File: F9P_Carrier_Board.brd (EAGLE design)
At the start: 88.9 x 41.9 mm, 93 parts, among them J4 U.FL, J5 QWIIC_RIGHT_ANGLE, J6 MICROMOD-2222-C, J8 JTAG, U1 U-BLOX_ZED-F9P, U5 AP7361C-33

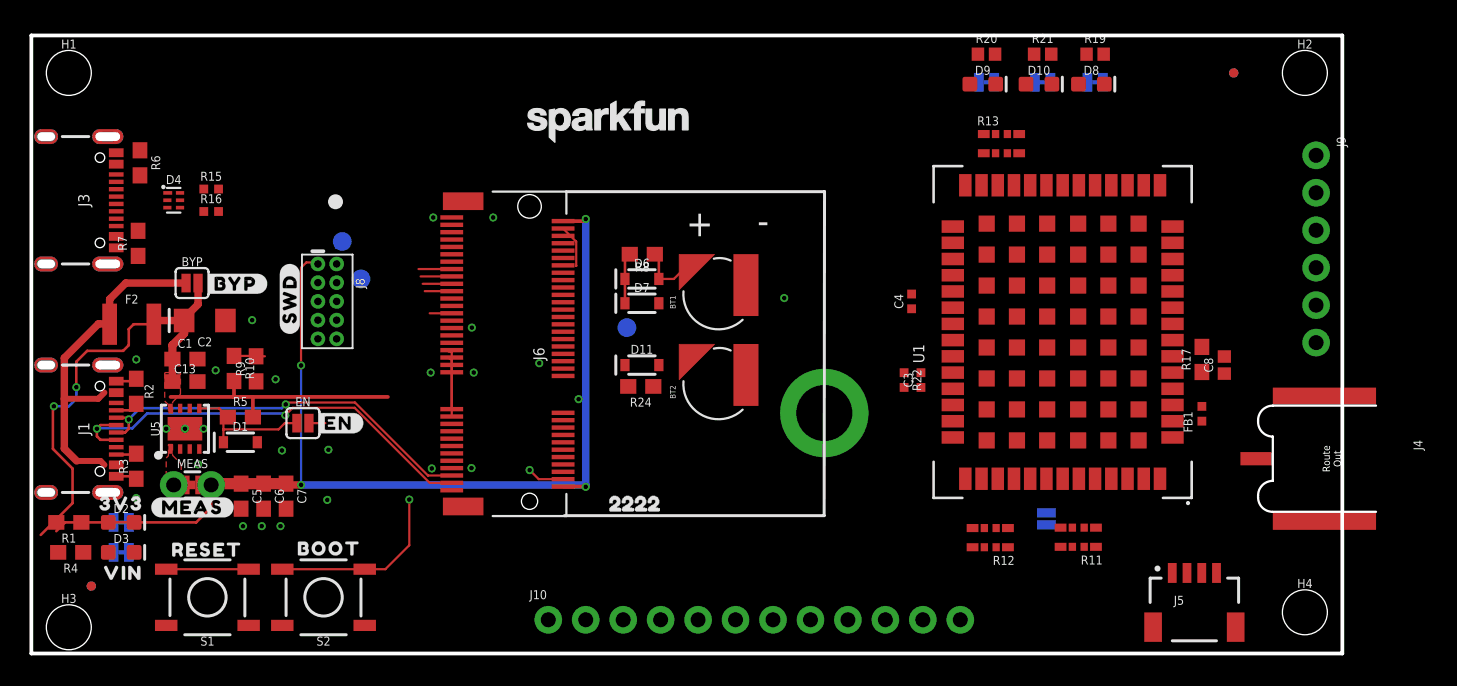
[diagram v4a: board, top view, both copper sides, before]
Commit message: Moves parts to their final resting places (mostly)
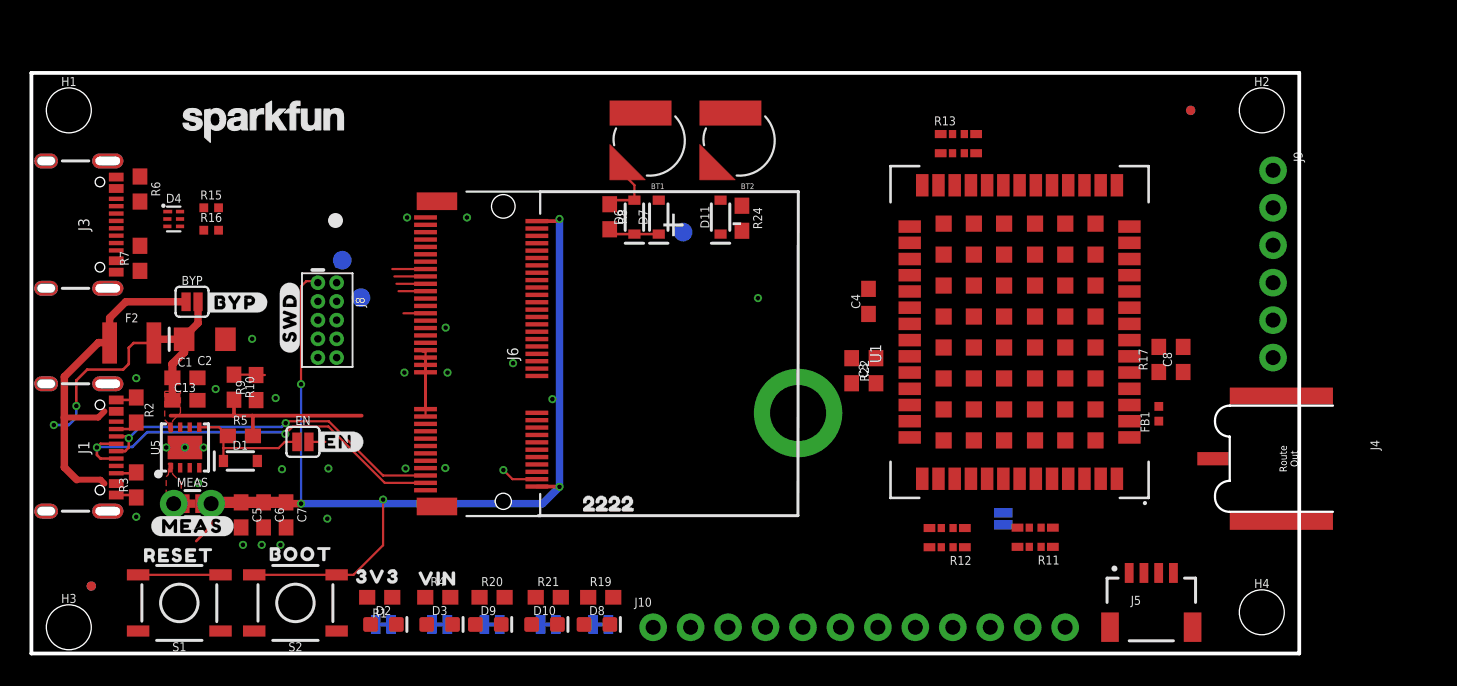
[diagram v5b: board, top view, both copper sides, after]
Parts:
- C3, C4: device SparkFun-Capacitors:0402-TIGHT -> SparkFun-Capacitors:0603
- C8: device SparkFun-Capacitors:0402 -> SparkFun-Capacitors:0603
- R19, R20, R21: value 1KOHM-0402-1/16W-1% -> 1k; device SparkFun-Resistors:0402 -> SparkFun-Resistors:0603
- R22: device SparkFun-Resistors:0402-TIGHT -> SparkFun-Resistors:0603
- moved R19 49.8 mm to (38.6, 3.81)
- moved R20 49.8 mm to (31.2, 3.81)
- moved R21 49.8 mm to (35.1, 3.81)
- moved GEOF 49.8 mm to (35.1, 1.97)
- moved PPS 49.8 mm to (38.6, 1.97)
- moved RTK 49.8 mm to (31.2, 1.97)
- moved D8 49.7 mm to (38.4, 1.97)
- moved D9 49.7 mm to (31.0, 1.97)
- moved D10 49.7 mm to (34.8, 1.97)
- moved R4 25.1 mm to (27.6, 3.81), turned to 0 degrees
- moved LOGO1 23.4 mm to (15.7, 36.1)
- moved D3 22.1 mm to (27.7, 1.97)
- moved VIN 22.1 mm to (27.7, 1.97), turned to 180 degrees
- moved R1 21.7 mm to (23.6, 3.81)
- moved U$68 21.3 mm to (27.6, 5.08)
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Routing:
- net VIN: track 48.2 -> 36.3 mm
- net 3.3V: track 76.4 -> 65.3 mm
- net RTC_3V: track 6.44 -> 3.51 mm
- net USB_N: track 26.9 -> 24.6 mm
- net USB_P: track 30.2 -> 27.9 mm
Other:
- board size 88.9 x 41.9 mm -> 86 x 39.4 mm

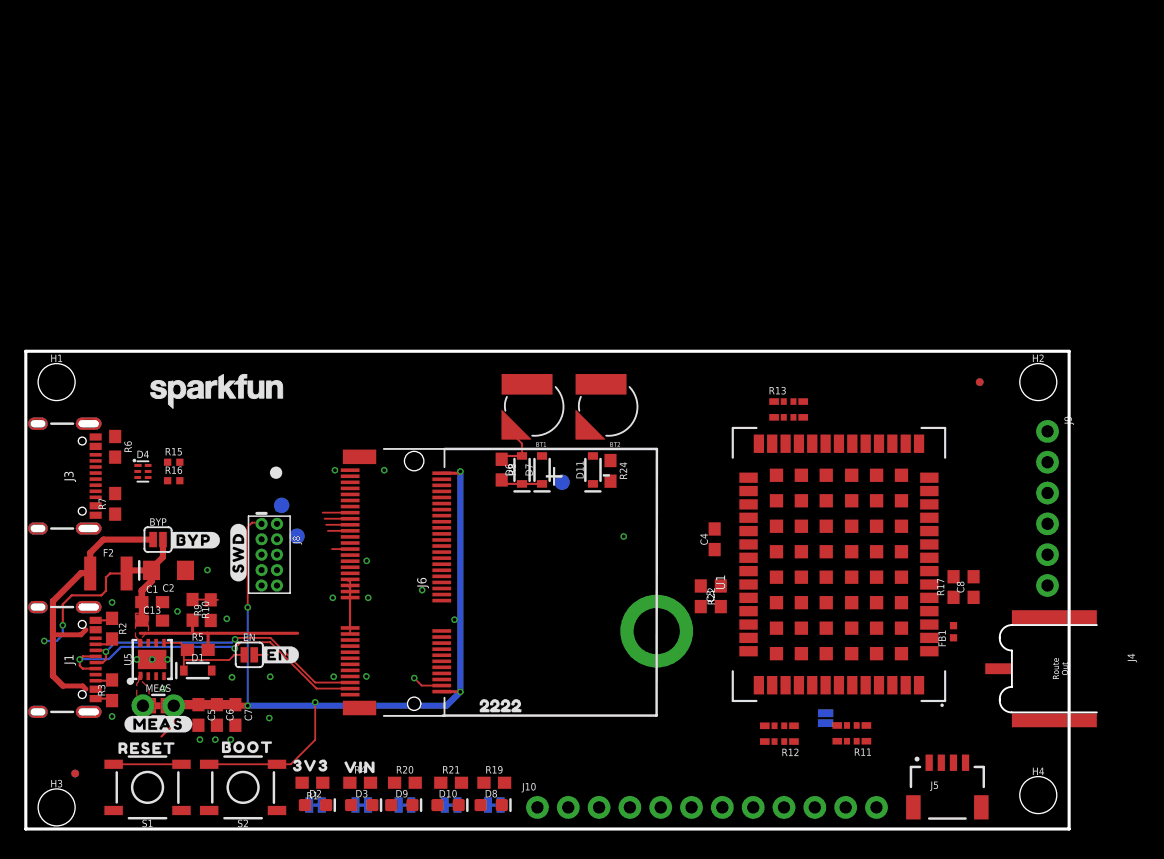
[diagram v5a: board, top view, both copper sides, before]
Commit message: Routes more air wires - almost done
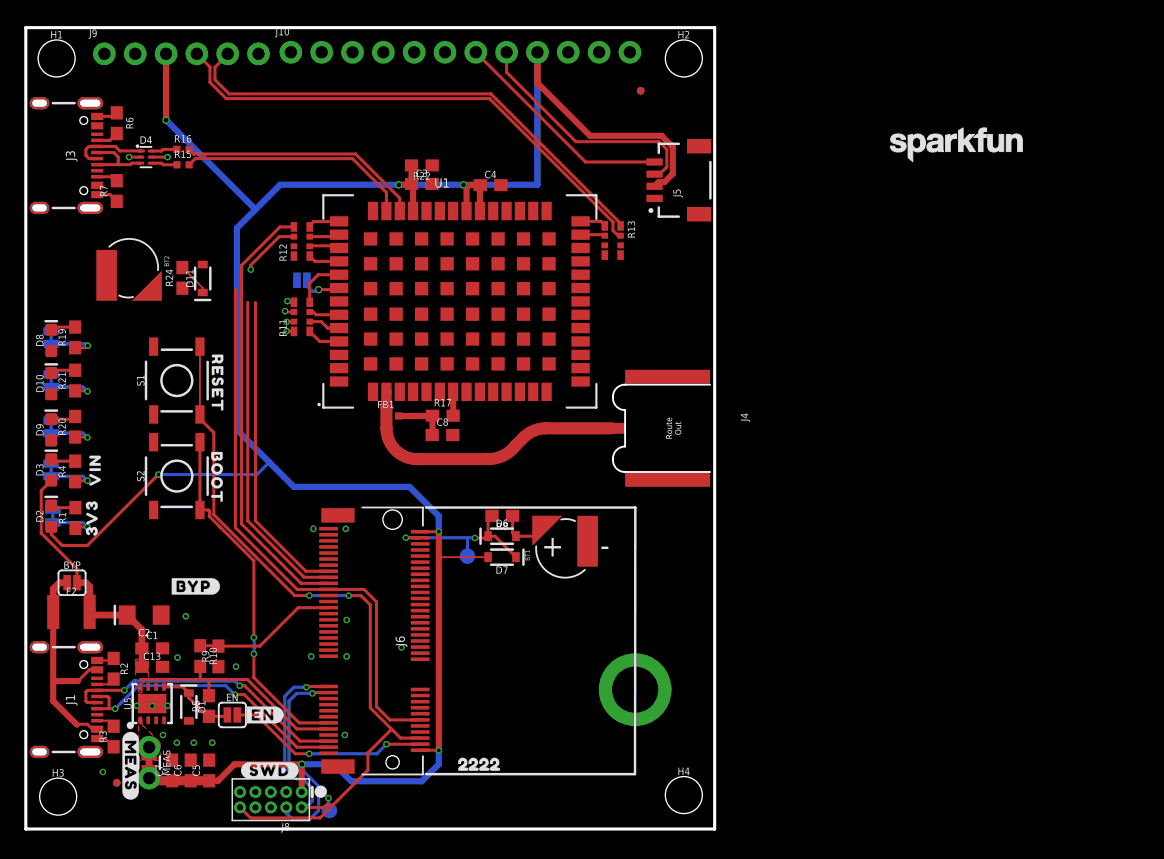
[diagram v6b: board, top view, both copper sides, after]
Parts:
- removed TP3: TEST-POINT3X5, SparkFun-Connectors:PAD.03X.05
- moved J9 83.7 mm to (6.48, 63.9), turned to 0 degrees
- moved J10 65.5 mm to (21.8, 64.0)
- moved LOGO1 64.3 mm to (76.7, 56.4)
- moved R11 56.8 mm to (22.8, 42.2), turned to 90 degrees
- moved R12 56.5 mm to (22.8, 48.4), turned to 90 degrees
- moved JP5 56.3 mm to (22.8, 45.2), turned to 0 degrees
- moved J5 53.7 mm to (51.8, 53.5), turned to 90 degrees
- moved PPS 53.1 mm to (2.10, 40.5), turned to 270 degrees
- moved D8 52.7 mm to (2.10, 40.3), turned to 90 degrees
- moved R19 50.4 mm to (4.06, 40.5), turned to 90 degrees
- moved FB1 49.5 mm to (30.2, 34.0), turned to 0 degrees
- moved GEOF 48.1 mm to (2.10, 37.0), turned to 270 degrees
- moved D10 47.7 mm to (2.10, 36.7), turned to 90 degrees
- moved C8 45.5 mm to (34.3, 32.5), turned to 0 degrees
- moved R21 45.4 mm to (4.06, 37.0), turned to 90 degrees
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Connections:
- removed net !SAFEBOOT: J10.3
- removed net GEOF_STAT: D10.A
- net !SAFEBOOT!: now also J10.3
- net GEO_STAT: now also D10.A
- net GND: now also D4.2
- net N$12: now also D4.3; no longer D4.1
- net N$13: now also D4.1; no longer D4.3
- net N$17: now also R15.1; no longer R16.1
- net N$6: no longer D4.2
- net N$9: now also R16.1; no longer R15.1
- net RXI2: no longer J6.22
- net SWDCK: no longer TP3.P$1
- net TXO2: no longer J6.20
- net VIN: no longer J1.VBUS1, J1.VBUS2, J3.VBUS1, J3.VBUS2
- net V_USB: now also J1.VBUS1, J1.VBUS2, J3.VBUS1, J3.VBUS2
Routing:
- net 3.3V: track 65.3 -> 198.4 mm, vias 4 -> 7
- net SDA/!CS!: track 1.83 -> 71.6 mm, vias 0 -> 1
- net !RESET!: track 5.59 -> 60.6 mm, vias 0 -> 2
- net SCL/CLK: track 1.97 -> 54.6 mm
- net RXI2: track 0.00 -> 42.3 mm
- net TXO2: track 0.00 -> 41.1 mm
- net TXO/SDO: track 2.11 -> 26.6 mm
- net RXI/SDI: track 2.25 -> 25.7 mm
- net RF_IN: track 0.00 -> 22.1 mm
- net ZED_USB_N: track 0.00 -> 20.1 mm
- net ZED_USB_P: track 0.00 -> 19.2 mm
- net !BOOT!: track 12.7 -> 29.6 mm, vias 1 -> 2
- net SWDIO: track 4.71 -> 18.7 mm, vias 0 -> 2
- net SWDCK: track 4.26 -> 17.6 mm, vias 0 -> 1
- net N$5: track 3.64 -> 16.7 mm, vias 1 -> 2
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- added copper zone on layer 1, net RF_IN
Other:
- board size 86 x 39.4 mm -> 56.8 x 66 mm

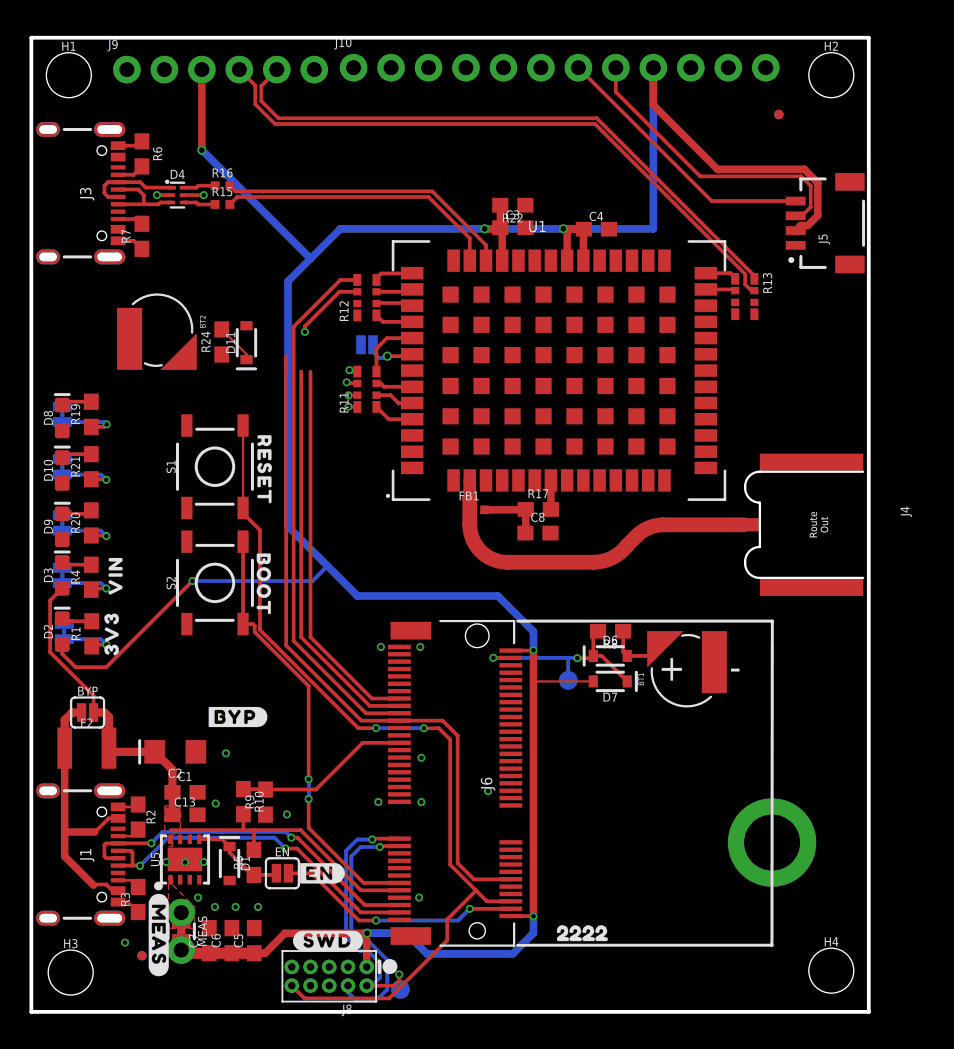
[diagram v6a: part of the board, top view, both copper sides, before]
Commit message: Finishes initial routing
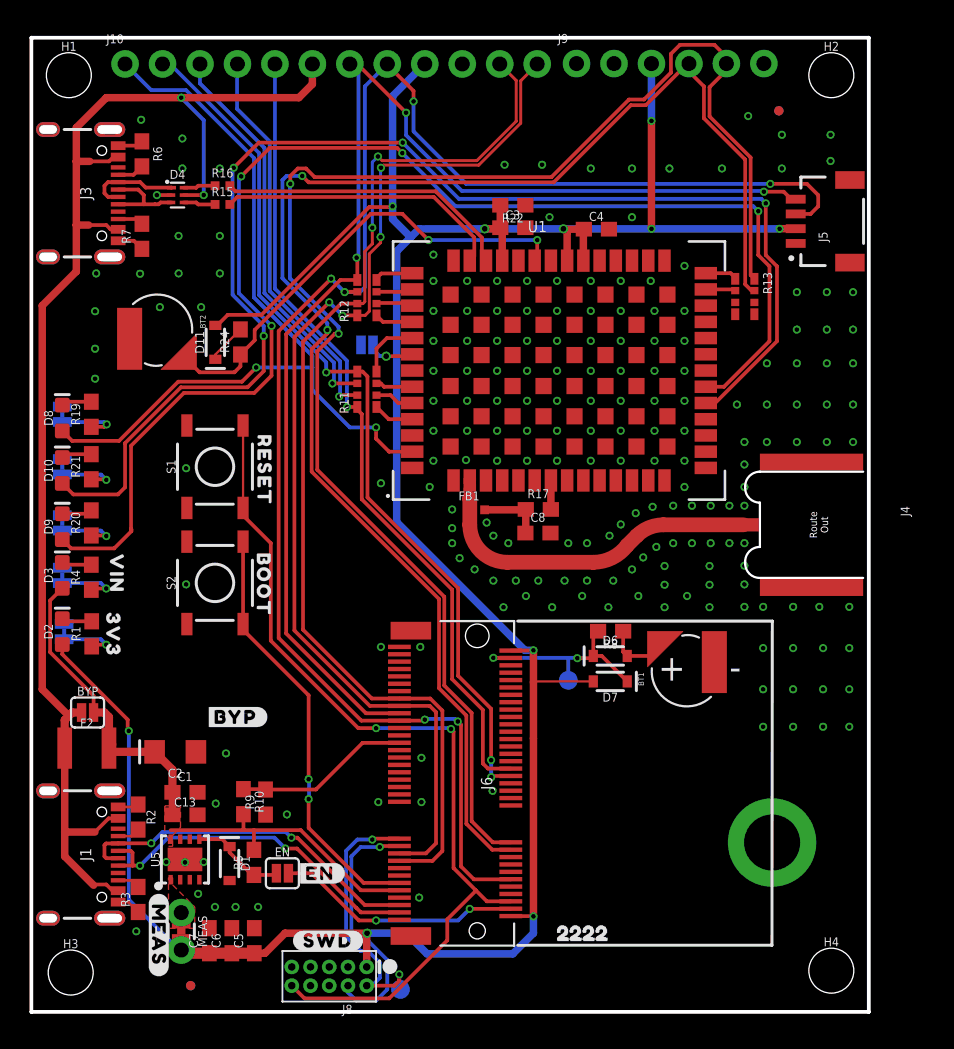
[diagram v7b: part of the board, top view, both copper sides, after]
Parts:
- moved J9 30.5 mm to (37.0, 64.3)
- moved J10 15.5 mm to (6.35, 64.3)
- moved FD1 3.88 mm to (10.8, 1.78)
- moved FD3 3.88 mm to (10.8, 1.78)
- moved D11 2.11 mm to (12.5, 45.4)
- moved R24 1.27 mm to (14.2, 45.4)
- moved FD2 0.25 mm to (50.7, 61.1)
- moved FD4 0.25 mm to (50.7, 61.1)
- moved U$68 0.15 mm to (5.79, 29.7), turned to 270 degrees
- moved J5 0.13 mm to (51.8, 53.6)
- moved U$69 0.11 mm to (5.54, 25.6), turned to 270 degrees
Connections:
- net INT: now also J6.40
- net RXI2: now also J6.20
- net TXO2: now also J6.22
- net TX_READY: now also J6.42
- net VIN: no longer D4.5, J10.6
- net V_USB: now also D4.5, J10.6
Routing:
- net RTK_STAT: track 0.00 -> 89.6 mm, vias 0 -> 4
- net GEO_STAT: track 0.00 -> 88.6 mm, vias 0 -> 4
- net V_USB: track 19.3 -> 94.0 mm, vias 0 -> 2
- net TXO2: track 41.1 -> 105.3 mm, vias 0 -> 2
- net INT: track 0.57 -> 60.8 mm, vias 1 -> 3
- net RXI2: track 42.3 -> 102.1 mm, vias 0 -> 2
- net PPS: track 0.00 -> 57.0 mm, vias 0 -> 2
- net TX_READY: track 0.60 -> 55.7 mm
- net RXI/SDI: track 25.7 -> 74.6 mm, vias 0 -> 2
- net TXO/SDO: track 26.6 -> 75.3 mm, vias 0 -> 4
- net SDA/!CS!: track 71.6 -> 110.6 mm, vias 1 -> 6
- net SCL/CLK: track 54.6 -> 86.5 mm, vias 0 -> 3
- net V_BATT: track 0.20 -> 32.0 mm, vias 0 -> 2
- net !SAFEBOOT!: track 0.75 -> 27.2 mm
- net !ZED_RESET!: track 0.60 -> 26.8 mm
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
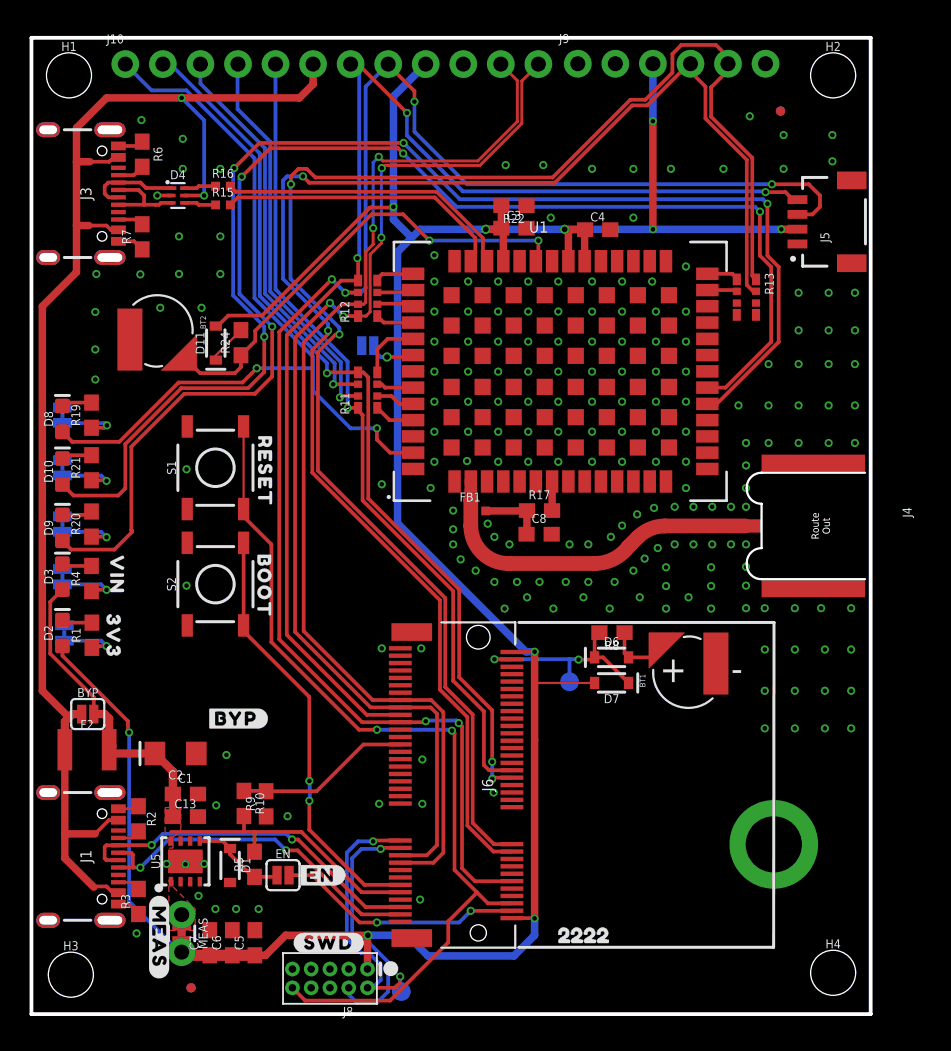
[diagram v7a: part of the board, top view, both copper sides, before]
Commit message: Adds more vias to the design
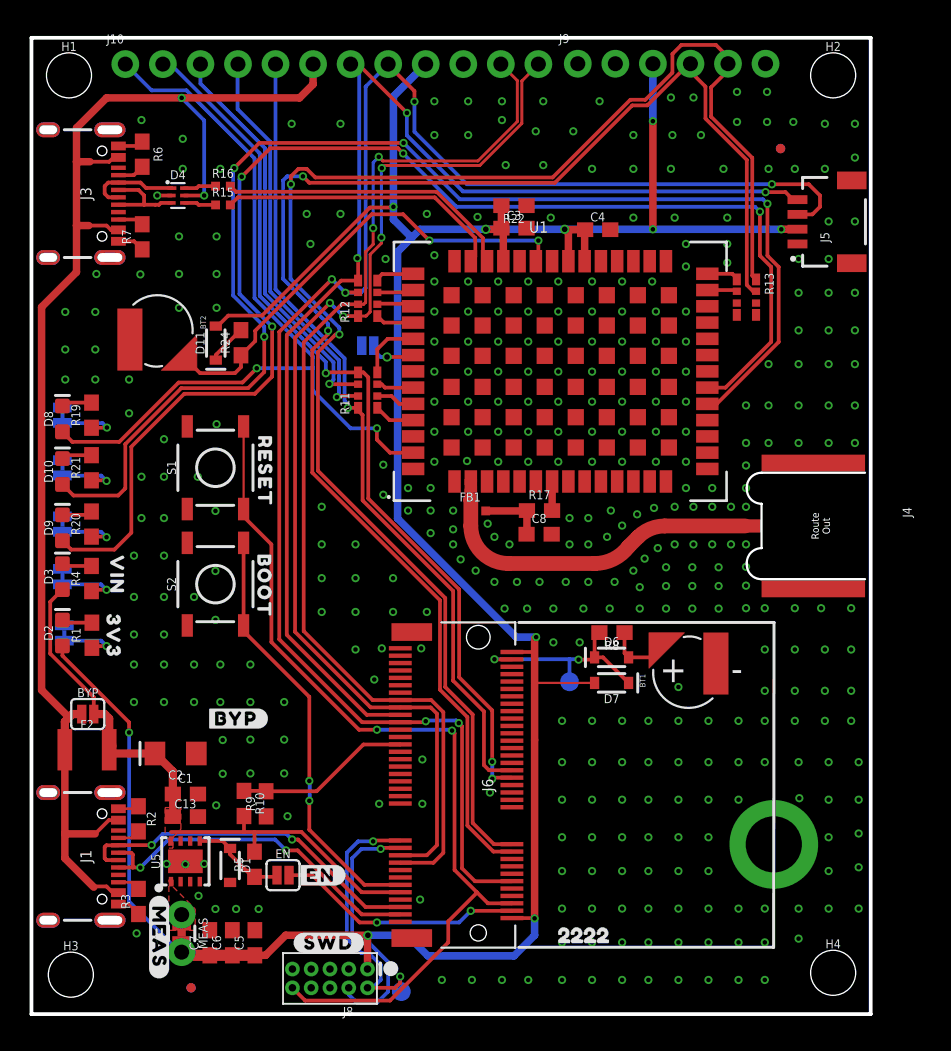
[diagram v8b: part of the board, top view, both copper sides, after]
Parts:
- moved FD2 2.54 mm to (50.7, 58.5)
- moved FD4 2.54 mm to (50.7, 58.5)
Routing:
- net 3.3V: track 188.9 -> 190.7 mm
- net GND: vias 203 -> 380
